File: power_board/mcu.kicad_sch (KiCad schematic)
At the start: 25 parts, among them J1 Conn_ARM_SWD_TagConnect_TC203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, U15 SM05B-GHS-TB(LF)(SN), U16 SM05B-GHS-TB(LF)(SN), U2 LM66100DCKR, U3 STM32L431KCUx

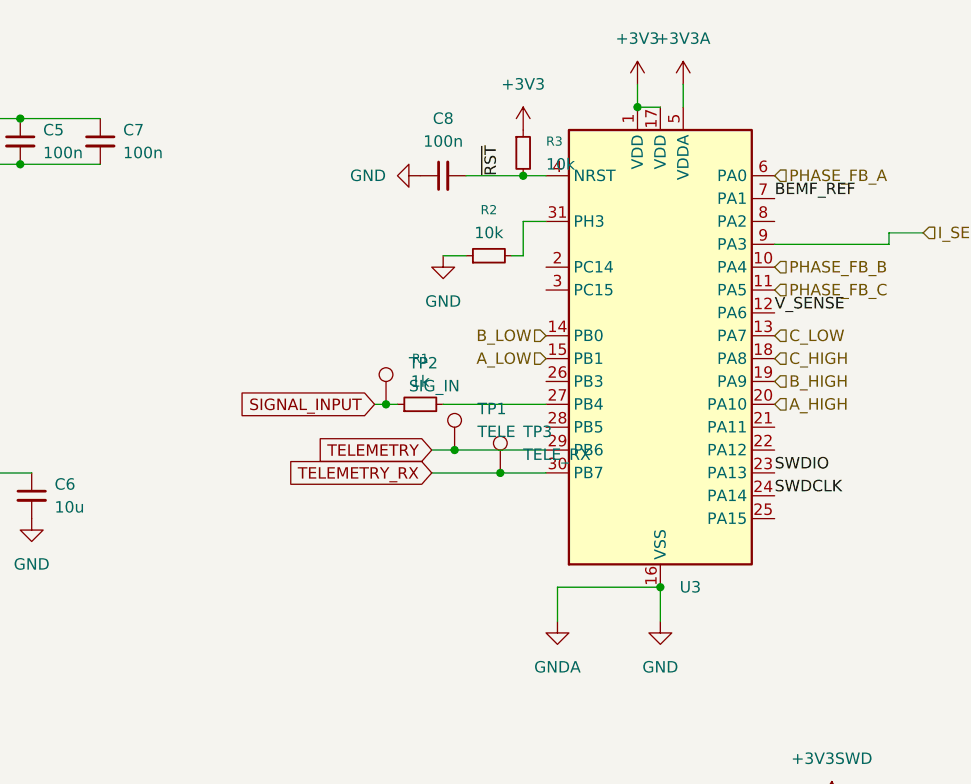
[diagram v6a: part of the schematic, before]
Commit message: change mcu to STM32F051K8U6
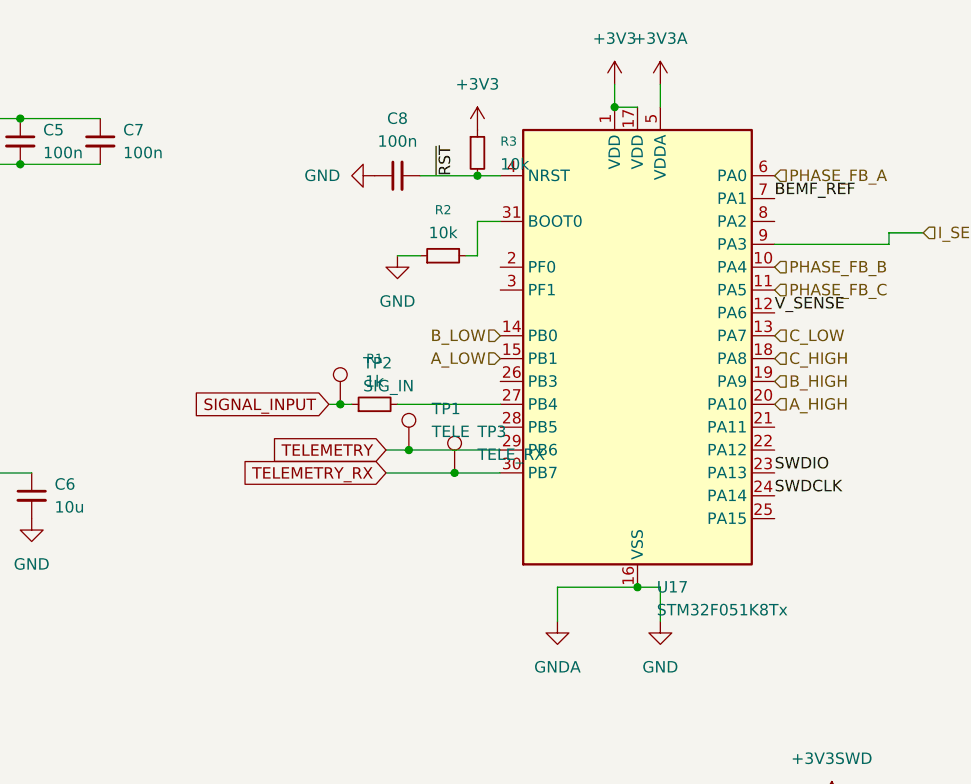
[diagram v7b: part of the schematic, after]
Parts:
- removed U3: STM32L431KCUx, Package_DFN_QFN:QFN-32-1EP_5x5mm_P0.5mm_EP3.1x3.1mm, symbol MCU_ST_STM32L4:STM32L431KCUx
- added U17: STM32F051K8Tx, Package_DFN_QFN:UFQFPN-32-1EP_5x5mm_P0.5mm_EP3.5x3.5mm, symbol MCU_ST_STM32F0:STM32F051K8Tx
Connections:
- net +3V3: now also U17.1 (VDD), U17.17 (VDD)
- net +3V3A: now also U17.5 (VDDA)
- net A_HIGH: now also U17.20 (PA10)
- net A_LOW: now also U17.15 (PB1)
- net BEMF_REF: now also U17.7 (PA1)
- net B_HIGH: now also U17.19 (PA9)
- net B_LOW: now also U17.14 (PB0)
- net C_HIGH: now also U17.18 (PA8)
- net C_LOW: now also U17.13 (PA7)
- net GND: now also U17.16 (VSS), U17.32 (VSS)
- net I_SENSE: now also U17.9 (PA3)
- net PHASE_FB_A : now also U17.6 (PA0)
- net PHASE_FB_B: now also U17.10 (PA4)
- net PHASE_FB_C: now also U17.11 (PA5)
- net SWDCLK: now also U17.24 (PA14)
- net SWDIO: now also U17.23 (PA13)
- net TELEMETRY: now also U17.29 (PB6)
- net TELEMETRY_RX: now also U17.30 (PB7)
- net V_SENSE: now also U17.12 (PA6)
- net ~{RST}: now also U17.4 (NRST)
- net at R1.2: now also U17.27 (PB4)
- net at R2.2: now also U17.31 (BOOT0)
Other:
- moved on the sheet: C8, R1, R2, R3, TP1, TP2, TP3
